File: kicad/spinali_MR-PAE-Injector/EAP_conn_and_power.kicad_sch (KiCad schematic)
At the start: 34 parts, among them J1 5055780421, J13 5055780421, J2 Conn_01x02_MountingPin, J6 Conn_01x03, Q1 BUK6D56-60EX, U1 LM74700, U3 LM5160DNTJ

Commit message: ongoing edits and prep
added symbols for 2 pin  and 3 pin headers.
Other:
- title: MR-T1-EAP Adapter -> MR-T1-PAE Injector
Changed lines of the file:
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@@
 	(paper "A4")
 	(title_block
-		(title "MR-T1-EAP Adapter")
+		(title "MR-T1-PAE Injector")
 		(date "2025-08-28")
 		(rev "X0")
@@
 		)
 		(instances
-			(project "flow_max"
+			(project "spinali_MR-PAE-Injector"
 				(path "/8b469ec1-e800-4d46-8a32-95d77ceae6db/cd546697-22c1-446e-bf49-97c1431cc780"
 					(reference "#PWR05")
@@
 		)
 		(instances
-			(project "flow_max"
+			(project "spinali_MR-PAE-Injector"
 				(path "/8b469ec1-e800-4d46-8a32-95d77ceae6db/cd546697-22c1-446e-bf49-97c1431cc780"
 					(reference "#PWR04")
@@
 		)
 		(instances
-			(project "flow_max"
+			(project "spinali_MR-PAE-Injector"
 				(path "/8b469ec1-e800-4d46-8a32-95d77ceae6db/cd546697-22c1-446e-bf49-97c1431cc780"
 					(reference "#PWR019")
@@
 		)
 		(instances
-			(project "spinali_mcxn_t1_hub"
+			(project "spinali_MR-PAE-Injector"
 				(path "/8b469ec1-e800-4d46-8a32-95d77ceae6db/cd546697-22c1-446e-bf49-97c1431cc780"
 					(reference "C2")
@@
 		)
 		(instances
-			(project "flow_max"
+			(project "spinali_MR-PAE-Injector"
 				(path "/8b469ec1-e800-4d46-8a32-95d77ceae6db/cd546697-22c1-446e-bf49-97c1431cc780"
 					(reference "R3")
@@
 		)
 		(instances
-			(project "spinali_mcxn_t1_hub"
+			(project "spinali_MR-PAE-Injector"
 				(path "/8b469ec1-e800-4d46-8a32-95d77ceae6db/cd546697-22c1-446e-bf49-97c1431cc780"
 					(reference "R6")
@@
 		)
 		(instances
-			(project "spinali_mcxn_t1_hub"
+			(project "spinali_MR-PAE-Injector"
 				(path "/8b469ec1-e800-4d46-8a32-95d77ceae6db/cd546697-22c1-446e-bf49-97c1431cc780"
 					(reference "#PWR022")
@@
 		)
 		(instances
-			(project "flow_max"
+			(project "spinali_MR-PAE-Injector"
 				(path "/8b469ec1-e800-4d46-8a32-95d77ceae6db/cd546697-22c1-446e-bf49-97c1431cc780"
 					(reference "#PWR030")
@@
 		)
 		(instances
-			(project ""
+			(project "spinali_MR-PAE-Injector"
 				(path "/8b469ec1-e800-4d46-8a32-95d77ceae6db/cd546697-22c1-446e-bf49-97c1431cc780"
 					(reference "D1")
@@
 		)
 		(instances
-			(project ""
+			(project "spinali_MR-PAE-Injector"
 				(path "/8b469ec1-e800-4d46-8a32-95d77ceae6db/cd546697-22c1-446e-bf49-97c1431cc780"
 					(reference "R8")
@@
 		)
 		(instances
-			(project ""
+			(project "spinali_MR-PAE-Injector"
 				(path "/8b469ec1-e800-4d46-8a32-95d77ceae6db/cd546697-22c1-446e-bf49-97c1431cc780"
 					(reference "D3")
@@
 		)
 		(instances
-			(project "flow_max"
+			(project "spinali_MR-PAE-Injector"
 				(path "/8b469ec1-e800-4d46-8a32-95d77ceae6db/cd546697-22c1-446e-bf49-97c1431cc780"
 					(reference "#PWR02")
@@
 		)
 		(instances
-			(project "flow_max"
+			(project "spinali_MR-PAE-Injector"
 				(path "/8b469ec1-e800-4d46-8a32-95d77ceae6db/cd546697-22c1-446e-bf49-97c1431cc780"
 					(reference "C3")
@@
 		)
 		(instances
-			(project "flow_max"
+			(project "spinali_MR-PAE-Injector"
 				(path "/8b469ec1-e800-4d46-8a32-95d77ceae6db/cd546697-22c1-446e-bf49-97c1431cc780"
 					(reference "C10")
@@
 		)
 		(instances
-			(project "spinali_mcxn_t1_hub"
+			(project "spinali_MR-PAE-Injector"
 				(path "/8b469ec1-e800-4d46-8a32-95d77ceae6db/cd546697-22c1-446e-bf49-97c1431cc780"
 					(reference "#PWR021")
@@
 		)
 		(instances
-			(project "flow_max"
+			(project "spinali_MR-PAE-Injector"
 				(path "/8b469ec1-e800-4d46-8a32-95d77ceae6db/cd546697-22c1-446e-bf49-97c1431cc780"
 					(reference "C5")
@@
 		)
 		(instances
-			(project ""
+			(project "spinali_MR-PAE-Injector"
 				(path "/8b469ec1-e800-4d46-8a32-95d77ceae6db/cd546697-22c1-446e-bf49-97c1431cc780"
 					(reference "L1")
@@
 		)
 		(instances
-			(project "flow_max"
+			(project "spinali_MR-PAE-Injector"
 				(path "/8b469ec1-e800-4d46-8a32-95d77ceae6db/cd546697-22c1-446e-bf49-97c1431cc780"
 					(reference "#PWR07")
@@
 		)
 		(instances
-			(project ""
+			(project "spinali_MR-PAE-Injector"
 				(path "/8b469ec1-e800-4d46-8a32-95d77ceae6db/cd546697-22c1-446e-bf49-97c1431cc780"
 					(reference "#PWR01")
@@
 		)
 		(instances
-			(project "flow_max"
+			(project "spinali_MR-PAE-Injector"
 				(path "/8b469ec1-e800-4d46-8a32-95d77ceae6db/cd546697-22c1-446e-bf49-97c1431cc780"
 					(reference "#PWR025")
@@
 		)
 		(instances
-			(project "spinali_mcxn_t1_hub"
+			(project "spinali_MR-PAE-Injector"
 				(path "/8b469ec1-e800-4d46-8a32-95d77ceae6db/cd546697-22c1-446e-bf49-97c1431cc780"
 					(reference "#PWR06")
@@
 		)
 		(instances
-			(project ""
+			(project "spinali_MR-PAE-Injector"
 				(path "/8b469ec1-e800-4d46-8a32-95d77ceae6db/cd546697-22c1-446e-bf49-97c1431cc780"
 					(reference "L2")
@@
 		)
 		(instances
-			(project "flow_max"
+			(project "spinali_MR-PAE-Injector"
 				(path "/8b469ec1-e800-4d46-8a32-95d77ceae6db/cd546697-22c1-446e-bf49-97c1431cc780"
 					(reference "#PWR026")
@@
 		)
 		(instances
-			(project "flow_max"
+			(project "spinali_MR-PAE-Injector"
 				(path "/8b469ec1-e800-4d46-8a32-95d77ceae6db/cd546697-22c1-446e-bf49-97c1431cc780"
 					(reference "C4")
@@
 		)
 		(instances
-			(project "flow_max"
+			(project "spinali_MR-PAE-Injector"
 				(path "/8b469ec1-e800-4d46-8a32-95d77ceae6db/cd546697-22c1-446e-bf49-97c1431cc780"
 					(reference "#PWR024")
@@
 		)
 		(instances
-			(project "flow_max"
+			(project "spinali_MR-PAE-Injector"
 				(path "/8b469ec1-e800-4d46-8a32-95d77ceae6db/cd546697-22c1-446e-bf49-97c1431cc780"
 					(reference "#PWR03")
@@
 		)
 		(instances
-			(project "flow_max"
+			(project "spinali_MR-PAE-Injector"
 				(path "/8b469ec1-e800-4d46-8a32-95d77ceae6db/cd546697-22c1-446e-bf49-97c1431cc780"
 					(reference "R4")
@@
 		)
 		(instances
-			(project "spinali_MR-T1-EAP-Adapter"
+			(project "spinali_MR-PAE-Injector"
 				(path "/8b469ec1-e800-4d46-8a32-95d77ceae6db/cd546697-22c1-446e-bf49-97c1431cc780"
 					(reference "J13")
@@
 		)
 		(instances
-			(project "flow_max"
+			(project "spinali_MR-PAE-Injector"
 				(path "/8b469ec1-e800-4d46-8a32-95d77ceae6db/cd546697-22c1-446e-bf49-97c1431cc780"
 					(reference "C17")
@@
 		)
 		(instances
-			(project "flow_max"
+			(project "spinali_MR-PAE-Injector"
 				(path "/8b469ec1-e800-4d46-8a32-95d77ceae6db/cd546697-22c1-446e-bf49-97c1431cc780"
 					(reference "R7")
@@
 		)
 		(instances
-			(project ""
+			(project "spinali_MR-PAE-Injector"
 				(path "/8b469ec1-e800-4d46-8a32-95d77ceae6db/cd546697-22c1-446e-bf49-97c1431cc780"
 					(reference "R5")
@@
 		)
 		(instances
-			(project "flow_max"
+			(project "spinali_MR-PAE-Injector"
 				(path "/8b469ec1-e800-4d46-8a32-95d77ceae6db/cd546697-22c1-446e-bf49-97c1431cc780"
 					(reference "C16")
@@
 		)
 		(instances
-			(project ""
+			(project "spinali_MR-PAE-Injector"
 				(path "/8b469ec1-e800-4d46-8a32-95d77ceae6db/cd546697-22c1-446e-bf49-97c1431cc780"
 					(reference "Q1")
@@
 		)
 		(instances
-			(project "flow_max"
+			(project "spinali_MR-PAE-Injector"
 				(path "/8b469ec1-e800-4d46-8a32-95d77ceae6db/cd546697-22c1-446e-bf49-97c1431cc780"
 					(reference "#PWR028")
@@
 		)
 		(instances
-			(project ""
+			(project "spinali_MR-PAE-Injector"
 				(path "/8b469ec1-e800-4d46-8a32-95d77ceae6db/cd546697-22c1-446e-bf49-97c1431cc780"
 					(reference "U1")
@@
 		)
 		(instances
-			(project ""
+			(project "spinali_MR-PAE-Injector"
 				(path "/8b469ec1-e800-4d46-8a32-95d77ceae6db/cd546697-22c1-446e-bf49-97c1431cc780"
 					(reference "J1")
@@
 		)
 		(instances
-			(project "flow_max"
+			(project "spinali_MR-PAE-Injector"
 				(path "/8b469ec1-e800-4d46-8a32-95d77ceae6db/cd546697-22c1-446e-bf49-97c1431cc780"
 					(reference "#PWR029")
@@
 		)
 		(instances
-			(project ""
+			(project "spinali_MR-PAE-Injector"
 				(path "/8b469ec1-e800-4d46-8a32-95d77ceae6db/cd546697-22c1-446e-bf49-97c1431cc780"
 					(reference "U3")
@@
 		)
 		(instances
-			(project "flow_max"
+			(project "spinali_MR-PAE-Injector"
 				(path "/8b469ec1-e800-4d46-8a32-95d77ceae6db/cd546697-22c1-446e-bf49-97c1431cc780"
 					(reference "#PWR016")
@@
 		)
 		(instances
-			(project "flow_max"
+			(project "spinali_MR-PAE-Injector"
 				(path "/8b469ec1-e800-4d46-8a32-95d77ceae6db/cd546697-22c1-446e-bf49-97c1431cc780"
 					(reference "#PWR020")
@@
 		)
 		(instances
-			(project "spinali_mcxn_t1_hub"
+			(project "spinali_MR-PAE-Injector"
 				(path "/8b469ec1-e800-4d46-8a32-95d77ceae6db/cd546697-22c1-446e-bf49-97c1431cc780"
 					(reference "C13")
@@
 		)
 		(instances
-			(project "flow_max"
+			(project "spinali_MR-PAE-Injector"
 				(path "/8b469ec1-e800-4d46-8a32-95d77ceae6db/cd546697-22c1-446e-bf49-97c1431cc780"
 					(reference "C11")
@@
 		)
 		(instances
-			(project "flow_max"
+			(project "spinali_MR-PAE-Injector"
 				(path "/8b469ec1-e800-4d46-8a32-95d77ceae6db/cd546697-22c1-446e-bf49-97c1431cc780"
 					(reference "#PWR027")
@@
 		)
 		(instances
-			(project "spinali_mcxn_t1_hub"
+			(project "spinali_MR-PAE-Injector"
 				(path "/8b469ec1-e800-4d46-8a32-95d77ceae6db/cd546697-22c1-446e-bf49-97c1431cc780"
 					(reference "C14")
@@
 		)
 		(instances
-			(project ""
+			(project "spinali_MR-PAE-Injector"
 				(path "/8b469ec1-e800-4d46-8a32-95d77ceae6db/cd546697-22c1-446e-bf49-97c1431cc780"
 					(reference "C9")
@@
 		)
 		(instances
-			(project "flow_max"
+			(project "spinali_MR-PAE-Injector"
 				(path "/8b469ec1-e800-4d46-8a32-95d77ceae6db/cd546697-22c1-446e-bf49-97c1431cc780"
 					(reference "#PWR018")
@@
 		)
 		(instances
-			(project "spinali_MR-T1-EAP-Adapter"
+			(project "spinali_MR-PAE-Injector"
 				(path "/8b469ec1-e800-4d46-8a32-95d77ceae6db/cd546697-22c1-446e-bf49-97c1431cc780"
 					(reference "#PWR0240")
@@
 		)
 		(instances
-			(project "spinali_mcxn_t1_hub"
+			(project "spinali_MR-PAE-Injector"
 				(path "/8b469ec1-e800-4d46-8a32-95d77ceae6db/cd546697-22c1-446e-bf49-97c1431cc780"
 					(reference "C12")
@@
 		)
 		(instances
-			(project ""
+			(project "spinali_MR-PAE-Injector"
 				(path "/8b469ec1-e800-4d46-8a32-95d77ceae6db/cd546697-22c1-446e-bf49-97c1431cc780"
 					(reference "C1")

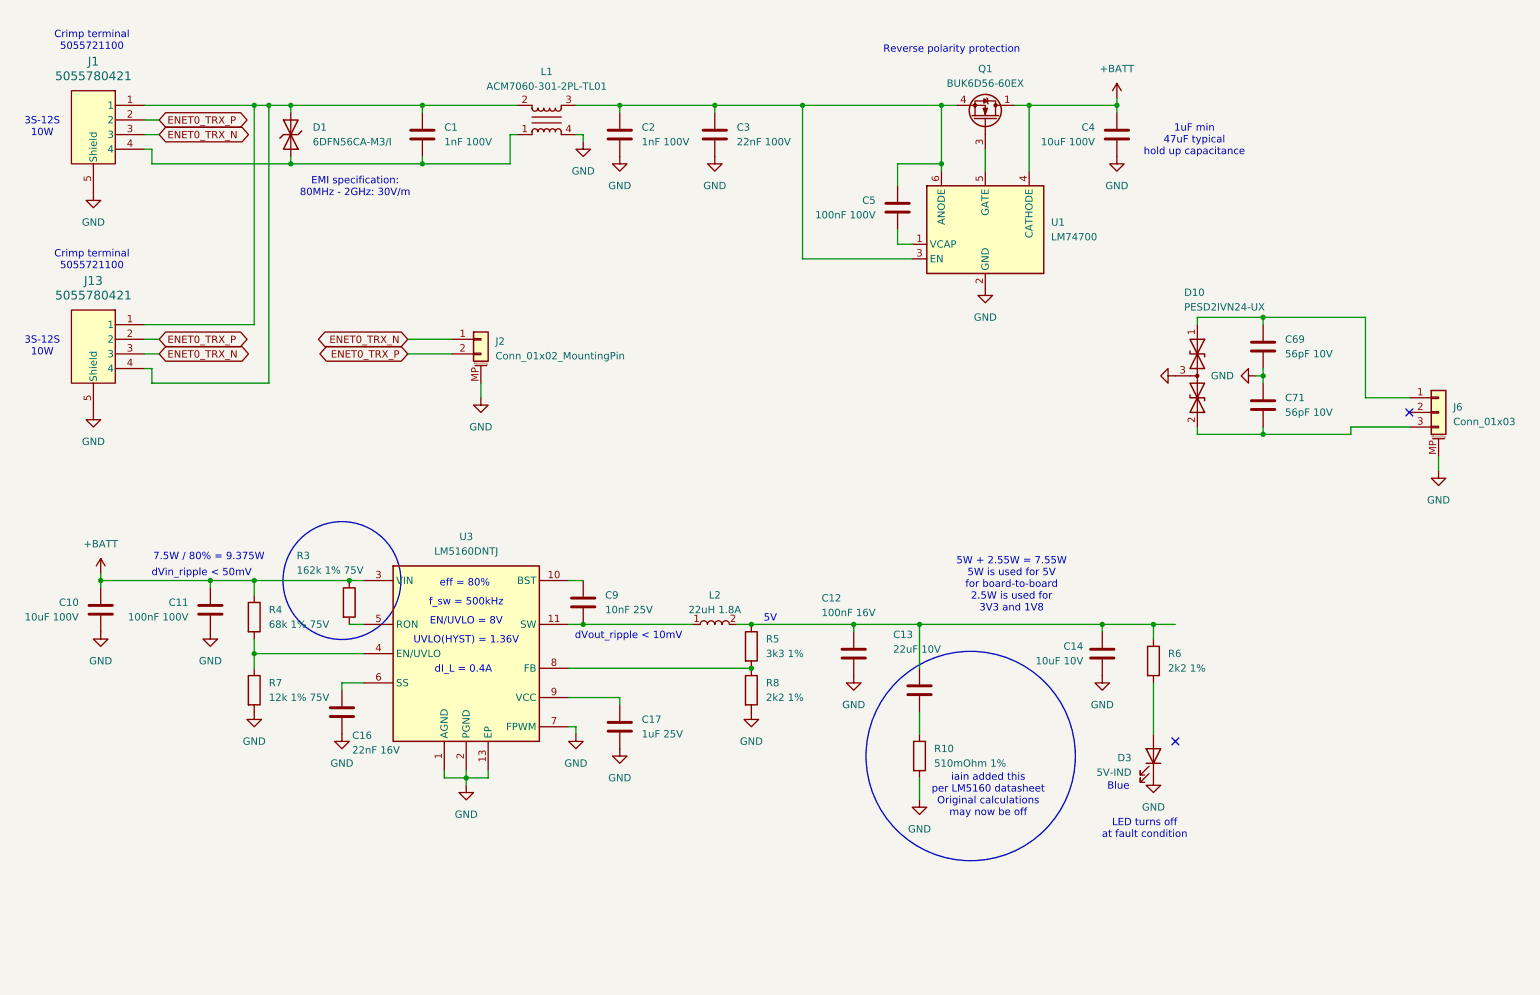
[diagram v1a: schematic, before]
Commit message: removed reverse polarity
MAY put it back in for the screw terminal connection.
Testing rough board sizes
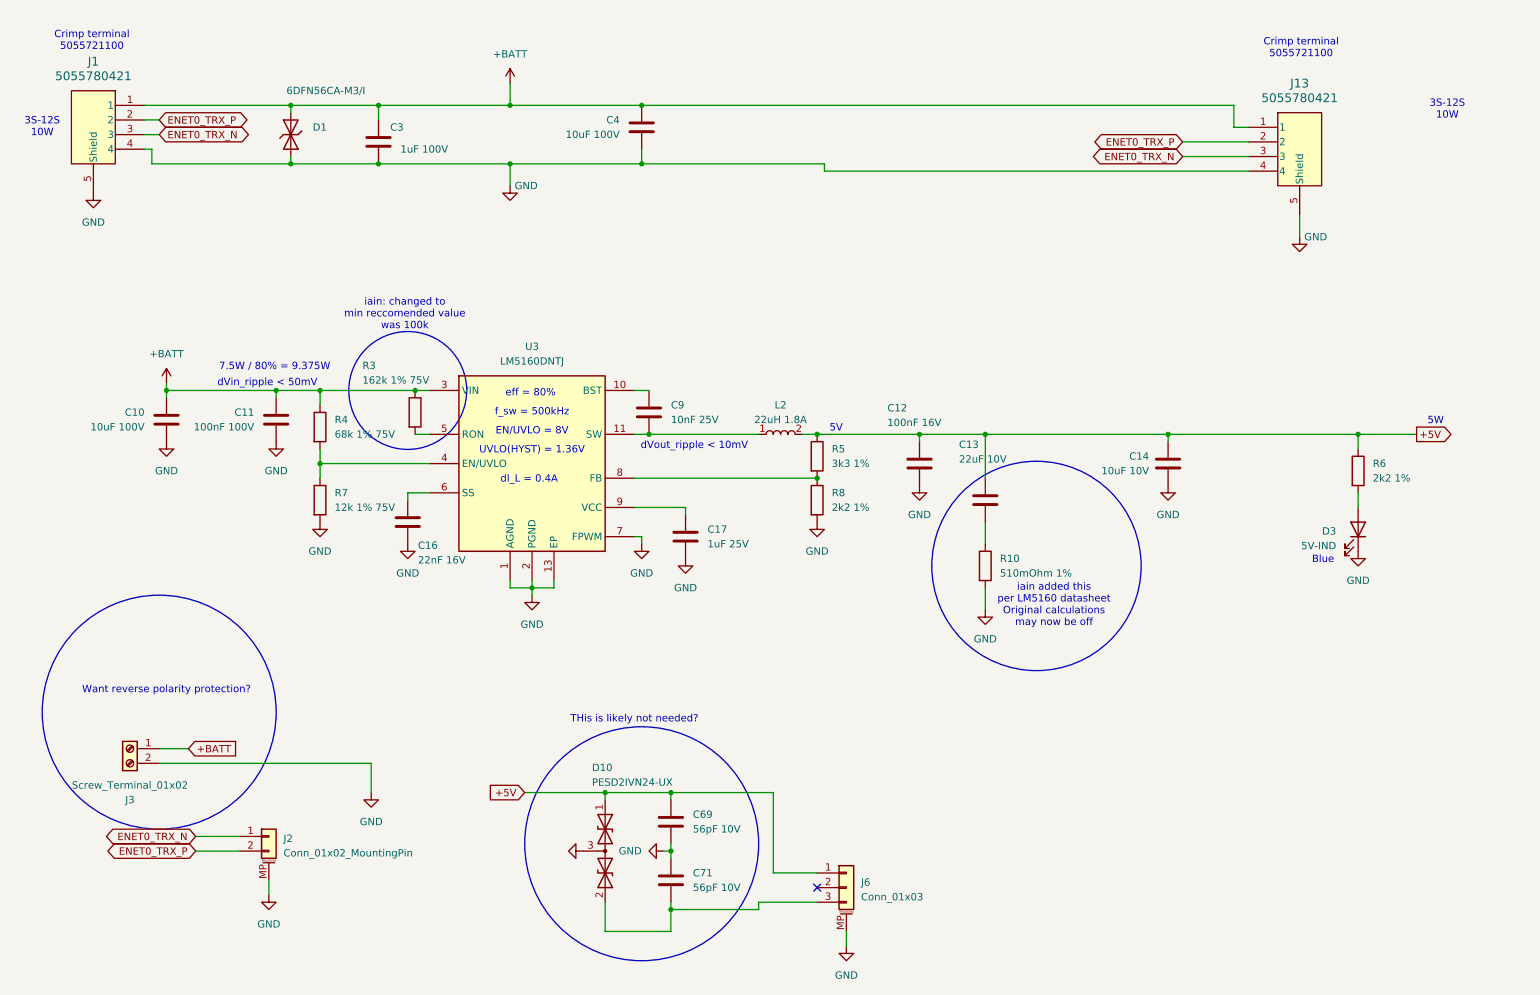
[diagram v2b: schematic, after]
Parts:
- removed C1, C2: 1nF 100V, Capacitor_SMD:C_0402_1005Metric, symbol Capacitors:GRM1885C2A102JA01D
- removed C5: 100nF 100V, Capacitor_SMD:C_0603_1608Metric, symbol Device:C
- removed L1: ACM7060-301-2PL-TL01, Inductors:ACM70603012PLTL01, symbol Inductors:ACM7060-301-2PL-TL01
- removed Q1: BUK6D56-60EX, MOSFETs:BUK6D5660EX, symbol MOSFETs:BUK6D56-60EX
- removed U1: LM74700, Package_TO_SOT_SMD:SOT-23-6, symbol Power_Management:LM74700
- added J3: Screw_Terminal_01x02, TerminalBlock_Phoenix:TerminalBlock_Phoenix_MKDS-1,5-2_1x02_P5.00mm_Horizontal, symbol Connector:Screw_Terminal_01x02
- C3: value 22nF 100V -> 1uF 100V
- J2: footprint (none) -> Connector_JST:JST_GH_SM02B-GHS-TB_1x02-1MP_P1.25mm_Horizontal
- J6: footprint (none) -> Connector_JST:JST_GH_SM03B-GHS-TB_1x03-1MP_P1.25mm_Horizontal
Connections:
- net +BATT: now also C3.2, D1.2, J1.1, J13.1, J3.1 (Pin_1)
- net GND: now also D1.1, J1.4, J13.4, J3.2 (Pin_2)
- net +5V: now reaches C12.1, C13.2, C14.2, L2.2, R5.1, R6.1
- net +5V: now also C69.1, D10.1 (A1), J6.1 (Pin_1)
- no-connect marks 2 -> 1
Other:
- note added: "5W"
- note added: "THis is likely not needed?"
- note added: "Want reverse polarity protection?"
- note added: "iain: changed to min reccomended value was 100k"
- note removed: "1uF min 47uF typical hold up capacitance"
- note removed: "5W + 2.55W = 7.55W 5W is used for 5V for board-to-board 2.5W is used for 3V3 and 1V8"
- note removed: "EMI specification: 80MHz - 2GHz: 30V/m"
- note removed: "LED turns off at fault condition"
- note removed: "Reverse polarity protection"
- moved on the sheet: C10, C11, C12, C13, C14, C16, C17, C3, C4, C69, C71, C9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

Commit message: Added reverse polarity protection.
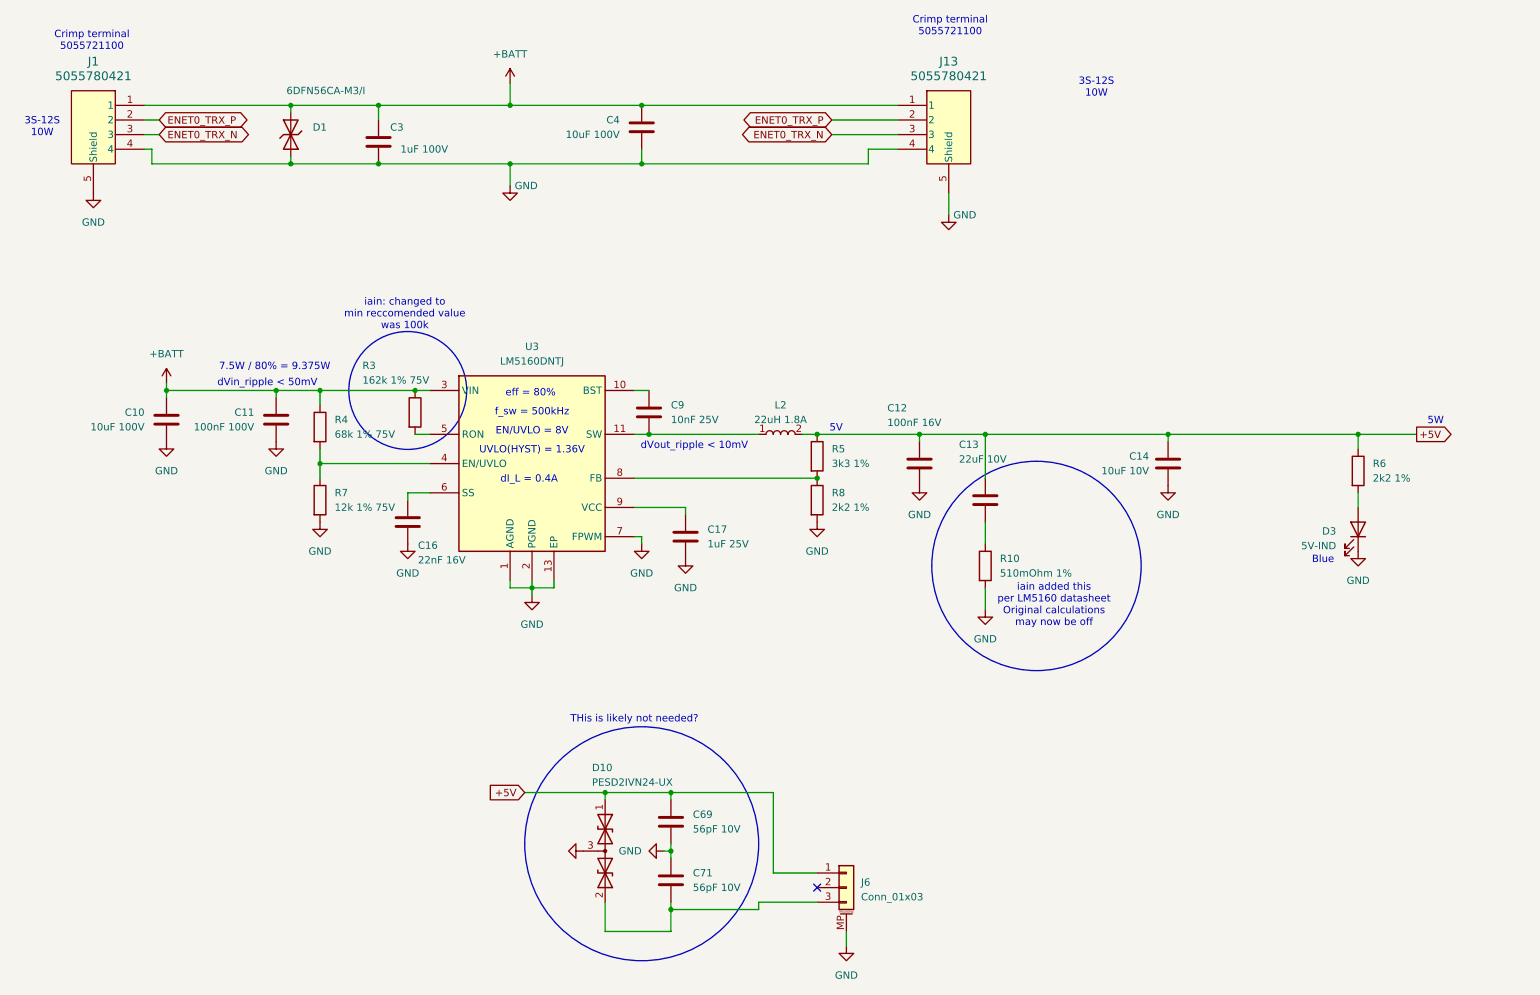
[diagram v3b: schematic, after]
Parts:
- removed J2: Conn_01x02_MountingPin, Connector_JST:JST_GH_SM02B-GHS-TB_1x02-1MP_P1.25mm_Horizontal, symbol Connector_Generic_MountingPin:Conn_01x02_MountingPin
- removed J3: Screw_Terminal_01x02, TerminalBlock_Phoenix:TerminalBlock_Phoenix_MKDS-1,5-2_1x02_P5.00mm_Horizontal, symbol Connector:Screw_Terminal_01x02
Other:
- note removed: "Want reverse polarity protection?"
- moved on the sheet: J13
